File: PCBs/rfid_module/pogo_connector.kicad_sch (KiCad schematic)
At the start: 4 parts, among them J401 10-Pin_Pogo_Connector_Male, Q203 DMN21D2UFB-7B

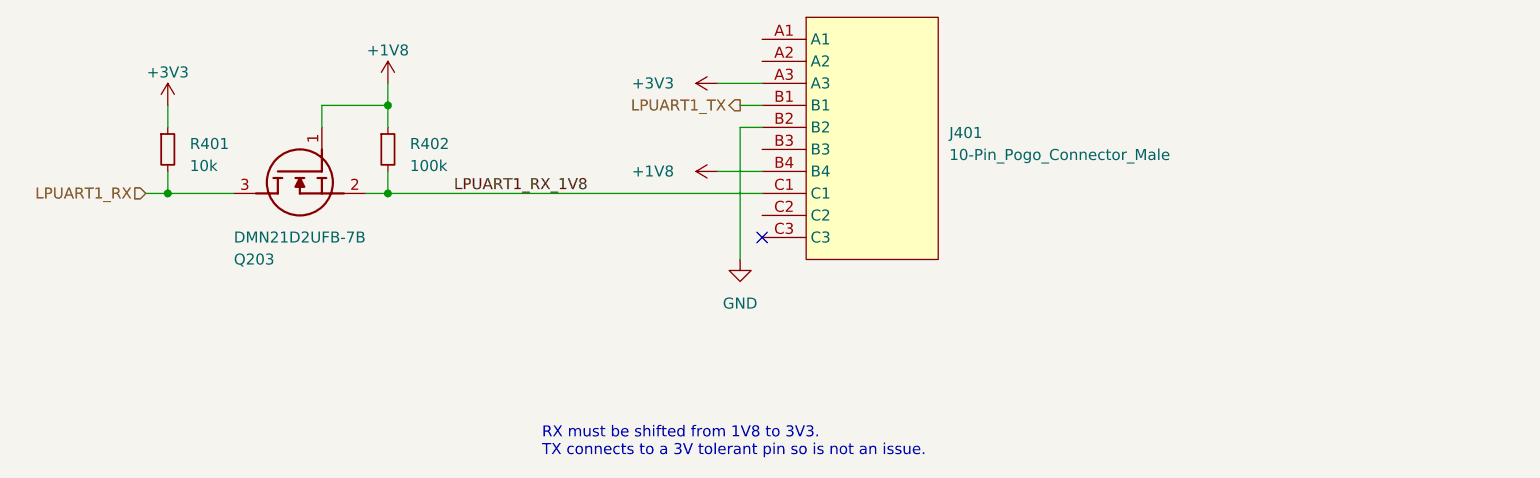
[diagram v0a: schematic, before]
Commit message: RFID PCB Done, started lower flex PCB
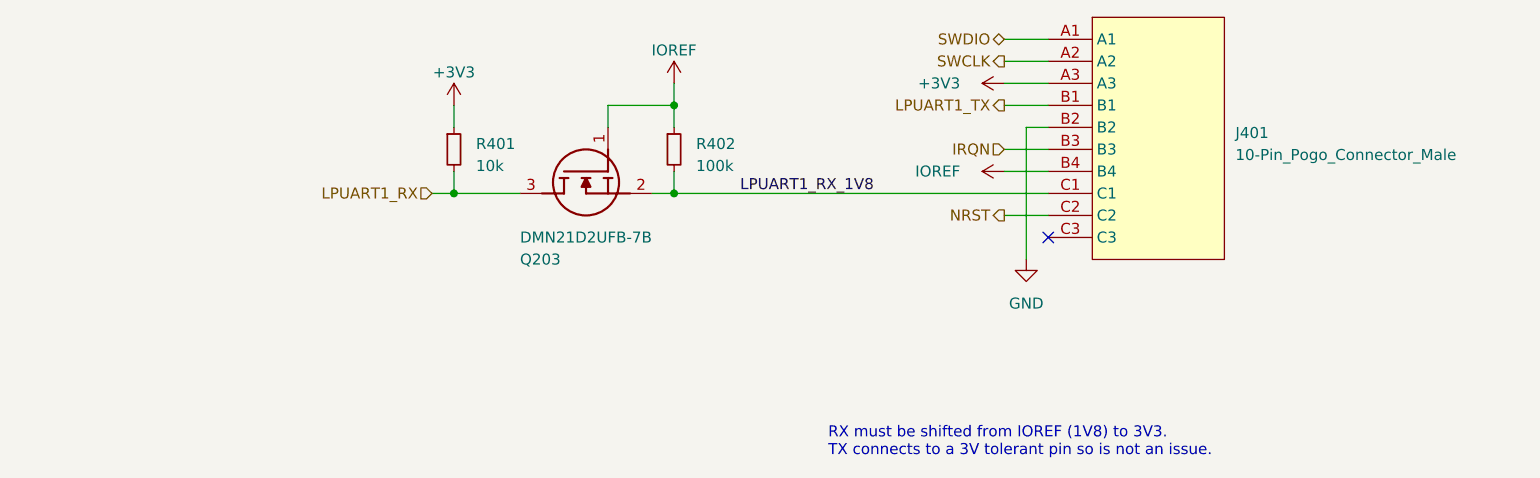
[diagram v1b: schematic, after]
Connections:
- net SWDIO: now reaches J401.A1
- net SWCLK: now reaches J401.A2
- net IRQN: now reaches J401.B3
- net NRST: now reaches J401.C2
- net +1V8 renamed IOREF
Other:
- note added: "RX must be shifted from IOREF (1V8) to 3V3. TX connects to a 3V tolerant pin so is not an issue."
- note removed: "RX must be shifted from 1V8 to 3V3. TX connects to a 3V tolerant pin so is not an issue."
- moved on the sheet: J401, Q203, R401, R402
